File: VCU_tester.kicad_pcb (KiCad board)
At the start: 2 copper layers, 200 x 159 mm, 125 parts, among them J1 Conn_01x04_Male, J10 DB9_Male, J11 DB9_Male, J12 Conn_01x08_Male, J13 Conn_01x08_Male, J14 USB_C_Receptacle, J15 USB_B_Micro, J16 Conn_01x05_Male, J2 Screw_Terminal_01x02, J3 DB9_Male, J4 DB9_Male, J5 DB9_Male, J500 Conn_01x10_Female, J501 Conn_01x08_Female, J502 Conn_01x08_Female, J503 Conn_01x08_Female, J504 Conn_01x08_Female, J505 Conn_01x08_Female, J507 Conn_02x18_Odd_Even, J6 DB9_Male, J7 Conn_01x04_Male, J8 DB9_Male, J9 DB9_Male, P8 BeagleBone_Black_Header, P9 BeagleBone_Black_Header, U1 REF3020, U2 MAX3232, U3 TCAN1042HVD, U4 MAX3232, U5 TCAN1042HVD, U6 DS3231MZ, U7 DS3231MZ

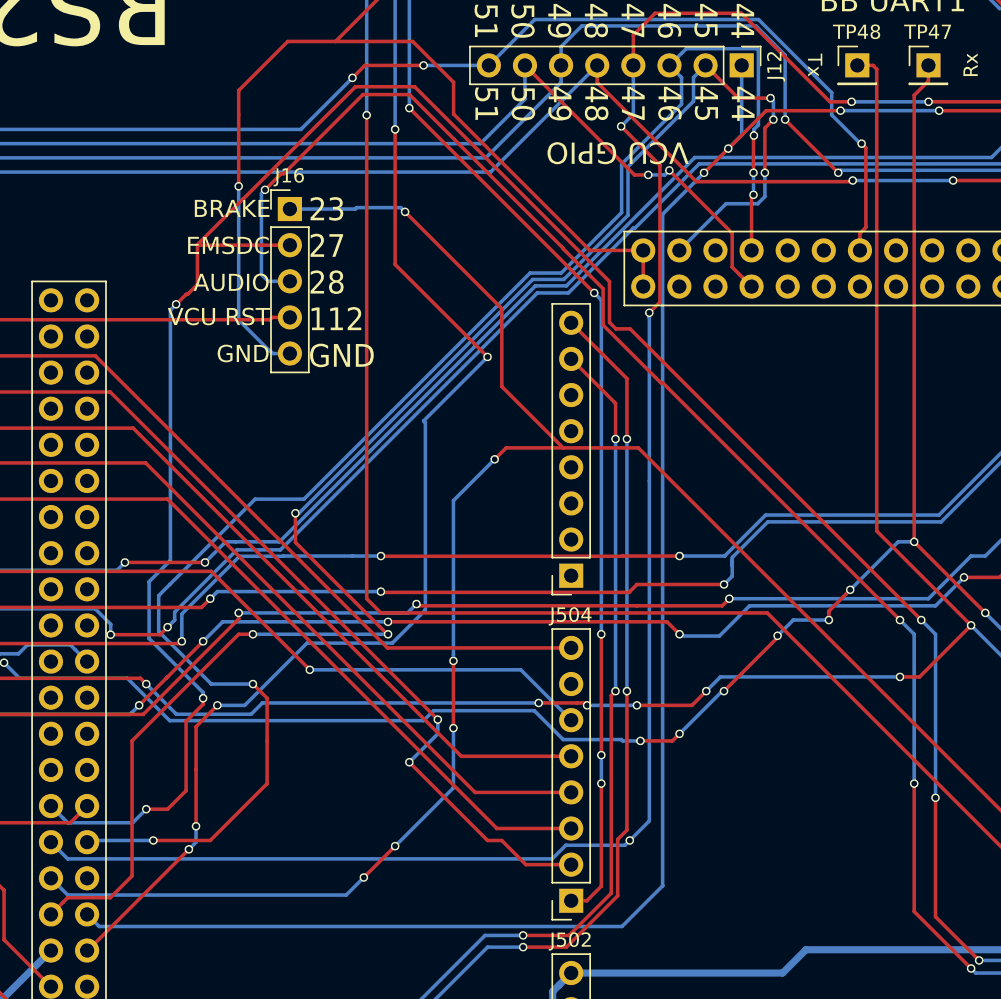
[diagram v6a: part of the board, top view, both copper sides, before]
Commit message: silkscreen, WE NEED TO CHECK CAN DB9
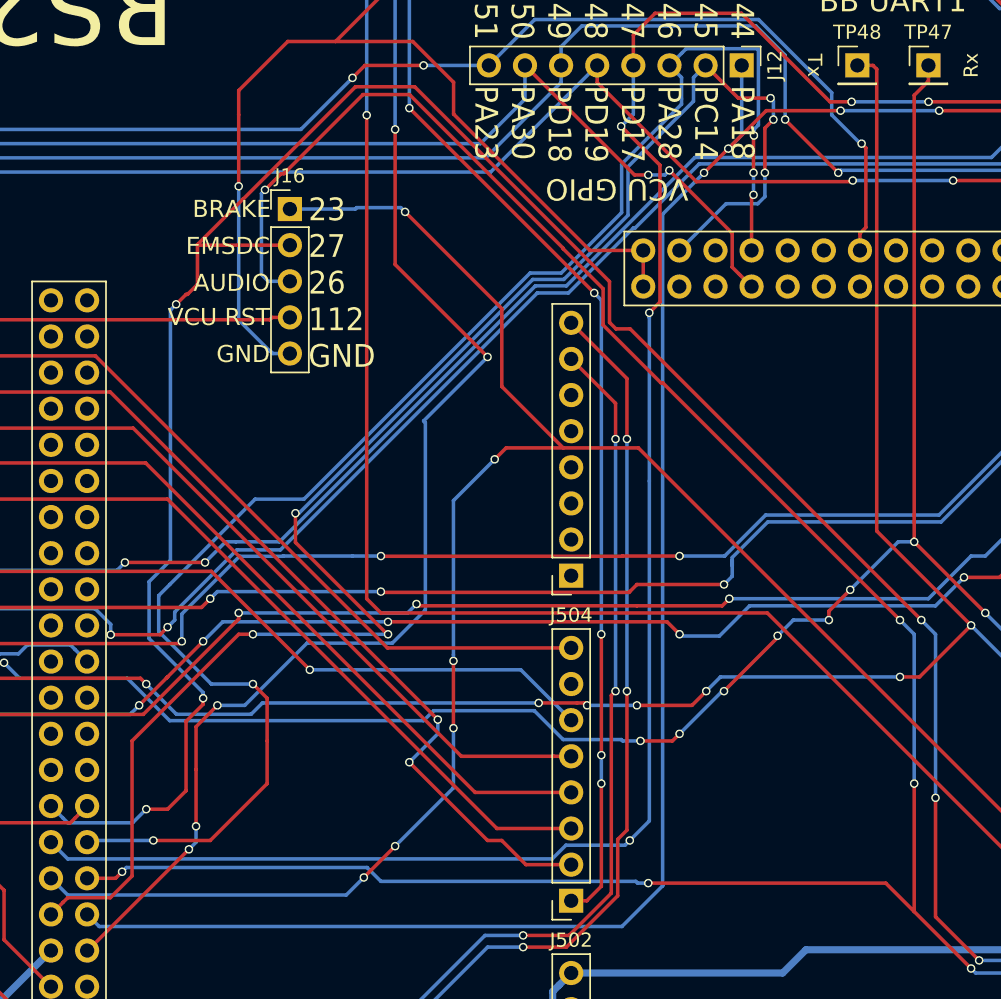
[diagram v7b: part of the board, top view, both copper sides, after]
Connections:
- J16 pad 3: /GPIO_28 -> /GPIO_26
- J503 pad 8: /GPIO_28 -> /GPIO_26
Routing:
- net /GPIO_26: track 0.00 -> 179.1 mm, vias 0 -> 6
- net /GPIO_28: track 119.3 -> 0.00 mm, vias 4 -> 0
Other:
- board text added: "23 27 26 112 GND"
- board text added: "PA18 PC14 PA28 PD17 PD19 PD18 PA30 PA23"
- board text removed: "23 27 28 112 GND"
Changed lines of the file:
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@@
     (thickness 1.6)
     (drawings 125)
-    (tracks 2103)
+    (tracks 2115)
     (zones 0)
     (modules 125)
-    (nets 256)
+    (nets 255)
   )
   (page A4)
@@
     (31 B.Cu signal)
     (32 B.Adhes user)
-    (33 F.Adhes user)
+    (33 F.Adhes user hide)
     (34 B.Paste user)
     (35 F.Paste user)
@@
   (net 253 /I2C1_SCL)
   (net 254 "Net-(J507-Pad27)")
-  (net 255 /GPIO_28)
   (net_class Default "To jest domyślna klasa połączeń."
     (clearance 0.2)
@@
     (add_net /GPIO_26)
     (add_net /GPIO_27)
-    (add_net /GPIO_28)
     (add_net /GPIO_44)
     (add_net /GPIO_45)
@@
       (net 25 /GPIO_112))
     (pad 3 thru_hole oval (at 0 5.08) (size 1.7 1.7) (drill 1) (layers *.Cu *.Mask)
-      (net 255 /GPIO_28))
+      (net 197 /GPIO_26))
     (pad 2 thru_hole oval (at 0 2.54) (size 1.7 1.7) (drill 1) (layers *.Cu *.Mask)
       (net 196 /GPIO_27))
@@
     (fp_line (start -1.27 -1.27) (end 0.635 -1.27) (layer F.Fab) (width 0.1))
     (pad 8 thru_hole oval (at 0 17.78) (size 1.7 1.7) (drill 1) (layers *.Cu *.Mask)
-      (net 255 /GPIO_28))
+      (net 197 /GPIO_26))
     (pad 7 thru_hole oval (at 0 15.24) (size 1.7 1.7) (drill 1) (layers *.Cu *.Mask)
       (net 196 /GPIO_27))
@@
     )
   )
-  (gr_text "23\n27\n28\n112\nGND" (at 123.9 52.8) (layer F.SilkS)
+  (gr_text "23\n27\n26\n112\nGND" (at 123.9 52.8) (layer F.SilkS)
     (effects (font (size 1.6 1.5) (thickness 0.2)) (justify left))
   )
-  (gr_text "VCU GPIO" (at 145.6299 43.6176 180) (layer F.SilkS)
+  (gr_text "VCU GPIO" (at 145.6 46.2 180) (layer F.SilkS)
     (effects (font (size 1.5 1.5) (thickness 0.3)))
   )
-  (gr_text "44\n45\n46\n47\n48\n49\n50\n51" (at 145.4 38.9 270) (layer F.SilkS)
+  (gr_text "PA18\nPC14\nPA28\nPD17\nPD19\nPD18\nPA30\nPA23" (at 145.4 38.9 270) (layer F.SilkS)
     (effects (font (size 1.6 1.5) (thickness 0.2)) (justify left))
   )
@@
   (segment (start 75.95 98.8) (end 76.25 98.5) (width 0.25) (layer F.Cu) (net 253))
   (segment (start 74.6 98.8) (end 75.95 98.8) (width 0.25) (layer F.Cu) (net 253))
-  (segment (start 190.64 101.32) (end 170.82 101.32) (width 0.25) (layer B.Cu) (net 255))
-  (via (at 166.5 88) (size 0.6) (drill 0.4) (layers F.Cu B.Cu) (net 255))
-  (via (at 170.5 101) (size 0.6) (drill 0.4) (layers F.Cu B.Cu) (net 255))
-  (segment (start 170.5 101) (end 166.5 97) (width 0.25) (layer F.Cu) (net 255))
-  (segment (start 170.82 101.32) (end 170.5 101) (width 0.25) (layer B.Cu) (net 255))
-  (segment (start 166.5 77.5) (end 165.5 76.5) (width 0.25) (layer B.Cu) (net 255))
-  (segment (start 166.5 88) (end 166.5 77.5) (width 0.25) (layer B.Cu) (net 255))
-  (via (at 165.5 76.5) (size 0.6) (drill 0.4) (layers F.Cu B.Cu) (net 255))
-  (segment (start 166.5 97) (end 166.5 88) (width 0.25) (layer F.Cu) (net 255))
-  (segment (start 148.814999 59.814999) (end 165.5 76.5) (width 0.25) (layer F.Cu) (net 255))
-  (segment (start 148.682789 59.814999) (end 148.814999 59.814999) (width 0.25) (layer F.Cu) (net 255))
-  (segment (start 144.625001 53.199999) (end 144.625002 55.757212) (width 0.25) (layer F.Cu) (net 255))
-  (segment (start 141.820602 50.360602) (end 141.820602 50.3956) (width 0.25) (layer F.Cu) (net 255))
-  (segment (start 144.625002 55.757212) (end 148.682789 59.814999) (width 0.25) (layer F.Cu) (net 255))
-  (segment (start 141.820602 50.3956) (end 144.625001 53.199999) (width 0.25) (layer F.Cu) (net 255))
-  (segment (start 127.738601 39.549991) (end 131.009991 39.549991) (width 0.25) (layer F.Cu) (net 255))
-  (segment (start 122.175001 45.113591) (end 127.738601 39.549991) (width 0.25) (layer F.Cu) (net 255))
-  (segment (start 131.009991 39.549991) (end 141.820602 50.360602) (width 0.25) (layer F.Cu) (net 255))
-  (segment (start 122.6 52.68) (end 121.08 52.68) (width 0.25) (layer B.Cu) (net 255))
-  (segment (start 121.08 52.68) (end 120.6 52.2) (width 0.25) (layer B.Cu) (net 255))
-  (segment (start 120.6 52.2) (end 120.6 46.498882) (width 0.25) (layer B.Cu) (net 255))
-  (via (at 120.849441 46.249441) (size 0.6) (drill 0.4) (layers F.Cu B.Cu) (net 255))
-  (segment (start 120.6 46.498882) (end 120.849441 46.249441) (width 0.25) (layer B.Cu) (net 255))
-  (segment (start 121.985291 45.113591) (end 122.175001 45.113591) (width 0.25) (layer F.Cu) (net 255))
-  (segment (start 120.849441 46.249441) (end 121.985291 45.113591) (width 0.25) (layer F.Cu) (net 255))
+  (segment (start 190.64 101.32) (end 170.82 101.32) (width 0.25) (layer B.Cu) (net 197))
+  (via (at 166.5 88) (size 0.6) (drill 0.4) (layers F.Cu B.Cu) (net 197))
+  (via (at 170.5 101) (size 0.6) (drill 0.4) (layers F.Cu B.Cu) (net 197))
+  (segment (start 170.5 101) (end 166.5 97) (width 0.25) (layer F.Cu) (net 197))
+  (segment (start 170.82 101.32) (end 170.5 101) (width 0.25) (layer B.Cu) (net 197))
+  (segment (start 166.5 77.5) (end 165.5 76.5) (width 0.25) (layer B.Cu) (net 197))
+  (segment (start 166.5 88) (end 166.5 77.5) (width 0.25) (layer B.Cu) (net 197))
+  (via (at 165.5 76.5) (size 0.6) (drill 0.4) (layers F.Cu B.Cu) (net 197))
+  (segment (start 166.5 97) (end 166.5 88) (width 0.25) (layer F.Cu) (net 197))
+  (segment (start 148.814999 59.814999) (end 165.5 76.5) (width 0.25) (layer F.Cu) (net 197))
+  (segment (start 148.682789 59.814999) (end 148.814999 59.814999) (width 0.25) (layer F.Cu) (net 197))
+  (segment (start 144.625001 53.199999) (end 144.625002 55.757212) (width 0.25) (layer F.Cu) (net 197))
+  (segment (start 141.820602 50.360602) (end 141.820602 50.3956) (width 0.25) (layer F.Cu) (net 197))
+  (segment (start 144.625002 55.757212) (end 148.682789 59.814999) (width 0.25) (layer F.Cu) (net 197))
+  (segment (start 141.820602 50.3956) (end 144.625001 53.199999) (width 0.25) (layer F.Cu) (net 197))
+  (segment (start 127.738601 39.549991) (end 131.009991 39.549991) (width 0.25) (layer F.Cu) (net 197))
+  (segment (start 122.175001 45.113591) (end 127.738601 39.549991) (width 0.25) (layer F.Cu) (net 197))
+  (segment (start 131.009991 39.549991) (end 141.820602 50.360602) (width 0.25) (layer F.Cu) (net 197))
+  (segment (start 122.6 52.68) (end 121.08 52.68) (width 0.25) (layer B.Cu) (net 197))
+  (segment (start 121.08 52.68) (end 120.6 52.2) (width 0.25) (layer B.Cu) (net 197))
+  (segment (start 120.6 52.2) (end 120.6 46.498882) (width 0.25) (layer B.Cu) (net 197))
+  (via (at 120.849441 46.249441) (size 0.6) (drill 0.4) (layers F.Cu B.Cu) (net 197))
+  (segment (start 120.6 46.498882) (end 120.849441 46.249441) (width 0.25) (layer B.Cu) (net 197))
+  (segment (start 121.985291 45.113591) (end 122.175001 45.113591) (width 0.25) (layer F.Cu) (net 197))
+  (segment (start 120.849441 46.249441) (end 121.985291 45.113591) (width 0.25) (layer F.Cu) (net 197))
+  (via (at 110.8 94.2) (size 0.6) (drill 0.4) (layers F.Cu B.Cu) (net 197))
+  (segment (start 108.34 94.66) (end 110.34 94.66) (width 0.25) (layer F.Cu) (net 197))
+  (segment (start 110.34 94.66) (end 110.8 94.2) (width 0.25) (layer F.Cu) (net 197))
+  (segment (start 129.000003 94.875001) (end 146.924999 94.875001) (width 0.25) (layer B.Cu) (net 197))
+  (segment (start 128.025003 93.900001) (end 129.000003 94.875001) (width 0.25) (layer B.Cu) (net 197))
+  (segment (start 110.8 94.2) (end 111.099999 93.900001) (width 0.25) (layer B.Cu) (net 197))
+  (segment (start 111.099999 93.900001) (end 128.025003 93.900001) (width 0.25) (layer B.Cu) (net 197))
+  (segment (start 146.924999 94.875001) (end 147.049998 95) (width 0.25) (layer B.Cu) (net 197))
+  (via (at 147.8 95) (size 0.6) (drill 0.4) (layers F.Cu B.Cu) (net 197))
+  (segment (start 147.049998 95) (end 147.8 95) (width 0.25) (layer B.Cu) (net 197))
+  (segment (start 164.5 95) (end 166.5 97) (width 0.25) (layer F.Cu) (net 197))
+  (segment (start 147.8 95) (end 164.5 95) (width 0.25) (layer F.Cu) (net 197))
 )

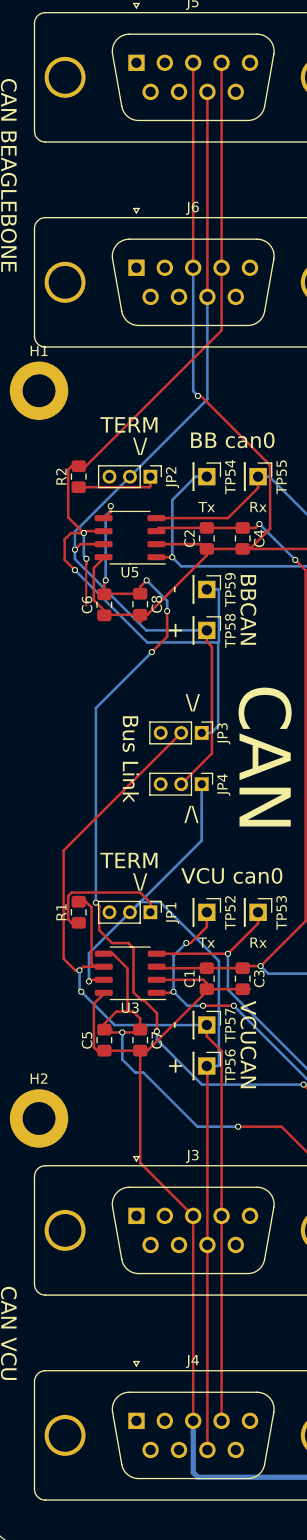
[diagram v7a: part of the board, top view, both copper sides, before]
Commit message: rs232/can fix
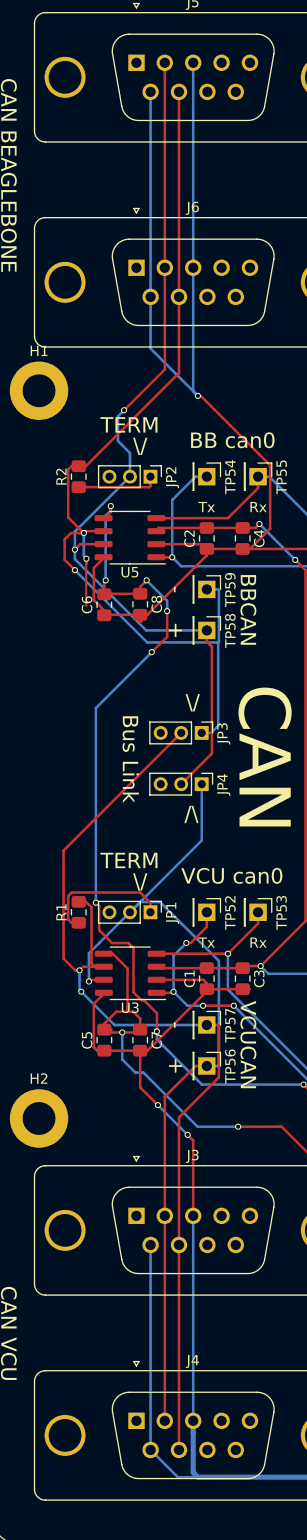
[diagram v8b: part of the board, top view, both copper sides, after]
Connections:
- J10 pad 5: Net-(J10-Pad5) -> GNDD
- J11 pad 5: Net-(J11-Pad5) -> GNDD
- J3 pad 2: Net-(J3-Pad2) -> VCUCAN+
- J3 pad 4: VCUCAN- -> Net-(J3-Pad4)
- J3 pad 6: Net-(J3-Pad6) -> GNDD
- J3 pad 7: Net-(J3-Pad7) -> VCUCAN-
- J3 pad 8: VCUCAN+ -> Net-(J3-Pad8)
- J4 pad 2: Net-(J4-Pad2) -> VCUCAN+
- J4 pad 4: VCUCAN- -> Net-(J4-Pad4)
- J4 pad 6: Net-(J4-Pad6) -> GNDD
- J4 pad 7: Net-(J4-Pad7) -> VCUCAN-
- J4 pad 8: VCUCAN+ -> Net-(J4-Pad8)
- J5 pad 2: Net-(J5-Pad2) -> BBCAN+
- J5 pad 4: BBCAN- -> Net-(J5-Pad4)
- J5 pad 6: Net-(J5-Pad6) -> GNDD
- J5 pad 7: Net-(J5-Pad7) -> BBCAN-
- J5 pad 8: BBCAN+ -> Net-(J5-Pad8)
- J6 pad 2: Net-(J6-Pad2) -> BBCAN+
- J6 pad 4: BBCAN- -> Net-(J6-Pad4)
- J6 pad 6: Net-(J6-Pad6) -> GNDD
- J6 pad 7: Net-(J6-Pad7) -> BBCAN-
- J6 pad 8: BBCAN+ -> Net-(J6-Pad8)
- J8 pad 5: Net-(J8-Pad5) -> GNDD
- J9 pad 5: Net-(J9-Pad5) -> GNDD
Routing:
- net GNDD: track 862.8 -> 920.1 mm, vias 19 -> 21
- net VCUCAN-: track 94.8 -> 99.8 mm
- net BBCAN-: track 101.7 -> 97.1 mm
- net BBCAN+: track 86.3 -> 88.3 mm, vias 1 -> 2
- net VCUCAN+: track 85.8 -> 85.2 mm
